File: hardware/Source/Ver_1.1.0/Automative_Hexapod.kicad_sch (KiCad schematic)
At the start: 0 parts

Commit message: update folder hardware
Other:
- added sheet HC-SR04 (HC-SR04.kicad_sch)
- added sheet IR Distance (IRDistance.kicad_sch)
- added sheet Level Shifting (LevelShifting.kicad_sch)
- added sheet Thermal Fan (ThermalFan.kicad_sch)

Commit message: update pcb v1.1.0
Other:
- removed sheet IR Distance
- added sheet Connector Servo (ConnectorServo.kicad_sch)
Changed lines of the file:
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@@
-	)
-	(sheet
-		(at 127 139.7)
-		(size 25.4 25.4)
-		(exclude_from_sim no)
-		(in_bom yes)
-		(on_board yes)
-		(dnp no)
-		(fields_autoplaced yes)
-		(stroke
-			(width 0.254)
-			(type solid)
-		)
-		(fill
-			(color 0 0 0 0.0000)
-		)
-		(property "Sheetname" "IR Distance"
-			(at 127 138.9376 0)
-			(effects
-				(font
-					(size 1.27 1.27)
-				)
-				(justify left bottom)
-			)
-		)
-		(property "Sheetfile" "IRDistance.kicad_sch"
-			(at 127 165.7354 0)
-			(effects
-				(font
-					(size 1.27 1.27)
-				)
-				(justify left top)
-			)
-		)
-		(instances
-			(project "Automative_Hexapod"
-				(path "/c07b6013-2147-4cef-a16e-342deb9ccbf5"
-					(page "8")
-				)
-			)
-		)
 	)
 	(sheet
@@
 			(project "Automative_Hexapod"
 				(path "/c07b6013-2147-4cef-a16e-342deb9ccbf5"
-					(page "4")
+					(page "6")
 				)
 			)
@@
 	)
 	(sheet
+		(at 292.1 139.7)
+		(size 25.4 25.4)
+		(exclude_from_sim no)
+		(in_bom yes)
+		(on_board yes)
+		(dnp no)
+		(fields_autoplaced yes)
+		(stroke
+			(width 0.254)
+			(type solid)
+		)
+		(fill
+			(color 0 0 0 0.0000)
+		)
+		(property "Sheetname" "Connector Servo"
+			(at 292.1 138.9376 0)
+			(effects
+				(font
+					(size 1.27 1.27)
+				)
+				(justify left bottom)
+			)
+		)
+		(property "Sheetfile" "ConnectorServo.kicad_sch"
+			(at 292.1 165.7354 0)
+			(effects
+				(font
+					(size 1.27 1.27)
+				)
+				(justify left top)
+			)
+		)
+		(instances
+			(project "Automative_Hexapod"
+				(path "/c07b6013-2147-4cef-a16e-342deb9ccbf5"
+					(page "9")
+				)
+			)
+		)
+	)
+	(sheet
 		(at 254 63.5)
 		(size 25.4 25.4)
@@
 			(project "Automative_Hexapod"
 				(path "/c07b6013-2147-4cef-a16e-342deb9ccbf5"
-					(page "6")
-				)
-			)
+					(page "4")
+				)
+			)

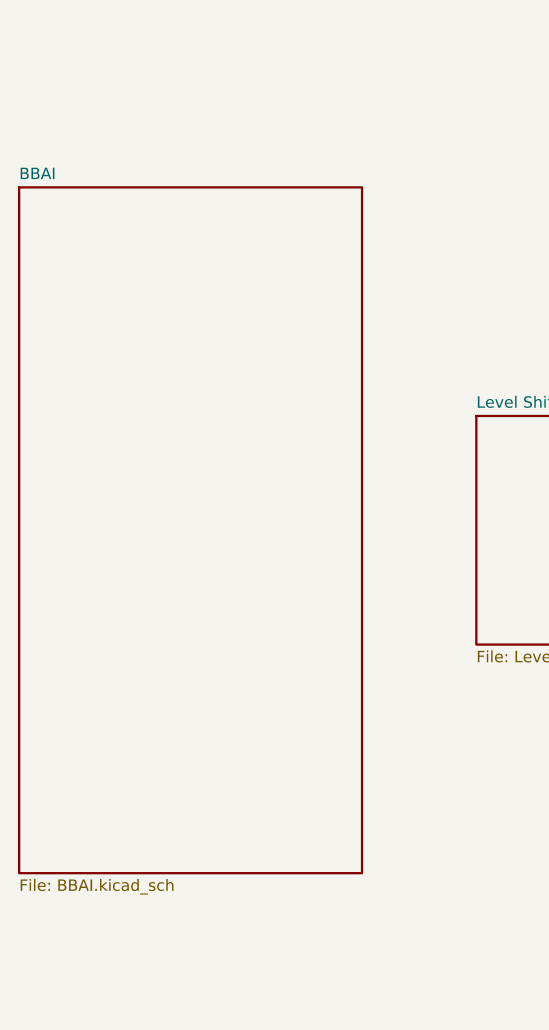
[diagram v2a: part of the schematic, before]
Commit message: Generate PDF Schematic Ver1.1.0 and add README.md
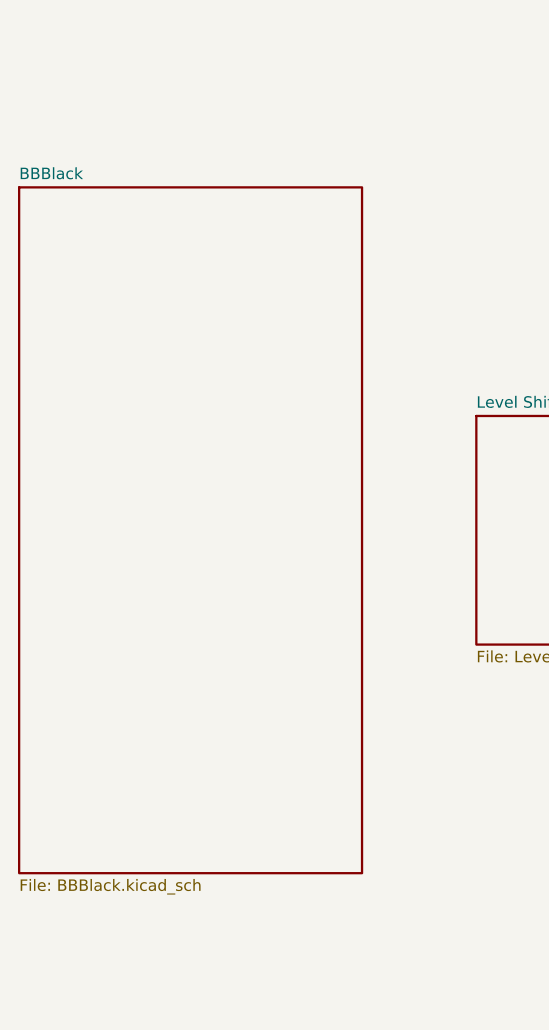
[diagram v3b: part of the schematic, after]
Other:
- sheet BBAI renamed BBBlack
- sheet BBBlack: file BBAI.kicad_sch -> BBBlack.kicad_sch
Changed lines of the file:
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@@
 			(color 0 0 0 0.0000)
 		)
-		(property "Sheetname" "BBAI"
+		(property "Sheetname" "BBBlack"
 			(at 165.1 113.5376 0)
 			(effects
@@
 			)
 		)
-		(property "Sheetfile" "BBAI.kicad_sch"
+		(property "Sheetfile" "BBBlack.kicad_sch"
 			(at 165.1 191.1354 0)
 			(effects
